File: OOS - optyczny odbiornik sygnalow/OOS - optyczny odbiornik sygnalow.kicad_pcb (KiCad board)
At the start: 2 copper layers, 25 x 50 mm, 45 parts, among them J101 Conn_Coaxial, J102 Conn_01x02_Socket, J103 Conn_01x02_Socket, J104 Conn_01x02_Socket, J105 Conn_01x02_Socket, U101 OPA300AIDBVR, U102 OPA300AIDBVR

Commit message: Polozenei komponentow na plycie, zdefiniowanie geometri, wczesny layout
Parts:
- removed C101, C104: 1p, Capacitor_SMD:C_0402_1005Metric
- removed C102: 2u2, Capacitor_SMD:C_0603_1608Metric
- removed C103: 100p, Capacitor_SMD:C_0402_1005Metric
- removed C105, C106: 1u, Resistor_SMD:R_0603_1608Metric
- removed C107, C108, C110: 100n, Resistor_SMD:R_0603_1608Metric
- removed C109, C111, C112: 10n, Capacitor_SMD:C_0402_1005Metric
- removed D101: BPX65, Package_TO_SOT_THT:TO-18-2_Lens
- removed D102, D103: LED, Diode_SMD:D_0603_1608Metric
- removed J101: Conn_Coaxial, Connector_Coaxial:BNC_Amphenol_B6252HB-NPP3G-50_Horizontal
- removed J102, J103, J104, J105: Conn_01x02_Socket, Connector_PinHeader_2.54mm:PinHeader_1x02_P2.54mm_Vertical
- removed JP101: SolderJumper_2_Open, Jumper:SolderJumper-2_P1.3mm_Bridged_RoundedPad1.0x1.5mm
- removed R101, R107, R108: 1k, Resistor_SMD:R_0402_1005Metric
- removed R102: 10, Resistor_SMD:R_0603_1608Metric
- removed R103, R104, R105, R109: 10k, Resistor_SMD:R_0402_1005Metric
- removed R106: 100, Resistor_SMD:R_0402_1005Metric
- removed R110: 10k, Resistor_SMD:R_0603_1608Metric
- removed R111: 2k2, Resistor_SMD:R_0603_1608Metric
- removed TP101, TP102, TP103, TP104, TP105, TP106, TP107, TP108, TP109, TP110, TP111: TestPoint_Small, TestPoint:TestPoint_Pad_D1.0mm
- removed U101, U102: OPA300AIDBVR, Package_TO_SOT_SMD:SOT-23-6_Handsoldering
- added C1: 1u, Resistor_SMD:R_0603_1608Metric, F.Cu at (194.3, 105.4)
- added C10: 1p, Capacitor_SMD:C_0402_1005Metric, F.Cu at (187.6, 102.4)
- added C11: 100p, Capacitor_SMD:C_0402_1005Metric, F.Cu at (187.1, 100.0)
- added C12: 1p, Capacitor_SMD:C_0402_1005Metric, F.Cu at (186.7, 89.4)
- added C2: 1u, Resistor_SMD:R_0603_1608Metric, F.Cu at (193.9, 93.9)
- added C3: 100n, Resistor_SMD:R_0603_1608Metric, F.Cu at (192.7, 105.4)
- added C4: 100n, Resistor_SMD:R_0603_1608Metric, F.Cu at (192.3, 93.9)
- added C5: 10n, Capacitor_SMD:C_0402_1005Metric, F.Cu at (191.4, 104.9)
- added C6: 10n, Capacitor_SMD:C_0402_1005Metric, F.Cu at (191.0, 93.4)
- added C7: 2u2, Capacitor_SMD:C_0603_1608Metric, F.Cu at (181.7, 108.3)
- added C8: 100n, Resistor_SMD:R_0603_1608Metric, F.Cu at (183.3, 108.3)
- added C9: 10n, Capacitor_SMD:C_0402_1005Metric, F.Cu at (184.6, 107.8)
- added D1: LED, Diode_SMD:D_0603_1608Metric, F.Cu at (179.8, 104.2)
- added D2: LED, Diode_SMD:D_0603_1608Metric, F.Cu at (197.2, 94.1)
- added D3: BPX65, Package_TO_SOT_THT:TO-18-2_Lens, F.Cu at (189.5, 110.1)
- added FID1: Fiducial, Fiducial:Fiducial_1.5mm_Mask3mm, F.Cu at (193.9, 115.4)
- added FID2: Fiducial, Fiducial:Fiducial_1.5mm_Mask3mm, F.Cu at (199.9, 82.9)
- added FID3: Fiducial, Fiducial:Fiducial_1.5mm_Mask3mm, F.Cu at (176.9, 82.9)
- added H1: MountingHole, MountingHole:MountingHole_3.2mm_M3, F.Cu at (176.9, 76.9)
- added H2: MountingHole, MountingHole:MountingHole_3.2mm_M3, F.Cu at (199.9, 76.9)
- added H3: MountingHole, MountingHole:MountingHole_3.2mm_M3, F.Cu at (199.9, 115.4)
- added H4: MountingHole, MountingHole:MountingHole_3.2mm_M3, F.Cu at (176.9, 115.4)
- added J1: Conn_01x02_Socket, Connector_PinHeader_2.54mm:PinHeader_1x02_P2.54mm_Vertical, F.Cu at (175.9, 107.0)
- added J2: Conn_01x02_Socket, Connector_PinHeader_2.54mm:PinHeader_1x02_P2.54mm_Vertical, F.Cu at (201.1, 97.0)
- added J3: Conn_01x02_Socket, Connector_PinHeader_2.54mm:PinHeader_1x02_P2.54mm_Vertical, F.Cu at (175.9, 97.0)
- added J4: Conn_01x02_Socket, Connector_PinHeader_2.54mm:PinHeader_1x02_P2.54mm_Vertical, F.Cu at (201.1, 107.0)
- added J5: Conn_Coaxial, Connector_Coaxial:BNC_Amphenol_B6252HB-NPP3G-50_Horizontal, F.Cu at (188.4, 84.5)
- added JP1: SolderJumper_2_Open, Jumper:SolderJumper-2_P1.3mm_Bridged_RoundedPad1.0x1.5mm, F.Cu at (201.1, 103.3)
- added R1: 10k, Resistor_SMD:R_0603_1608Metric, F.Cu at (176.7, 104.2)
- added R10: 1k, Resistor_SMD:R_0402_1005Metric, F.Cu at (187.2, 91.9)
- added R11: 1k, Resistor_SMD:R_0402_1005Metric, F.Cu at (188.1, 88.9)
- added R2: 2k2, Resistor_SMD:R_0603_1608Metric, F.Cu at (200.3, 94.1)
- added R3: 10, Resistor_SMD:R_0603_1608Metric, F.Cu at (179.4, 110.6)
- added R4: 10k, Resistor_SMD:R_0402_1005Metric, F.Cu at (198.8, 103.9)
- added R5: 10k, Resistor_SMD:R_0402_1005Metric, F.Cu at (182.9, 101.5)
- added R6: 10k, Resistor_SMD:R_0402_1005Metric, F.Cu at (182.9, 100.4)
- added R7: 10k, Resistor_SMD:R_0402_1005Metric, F.Cu at (182.9, 99.3)
- added R8: 1k, Resistor_SMD:R_0402_1005Metric, F.Cu at (187.6, 103.4)
- added R9: 100, Resistor_SMD:R_0402_1005Metric, F.Cu at (187.6, 97.4)
- added TP1: TestPoint_Small, TestPoint:TestPoint_Pad_D1.0mm, F.Cu at (178.6, 109.2)
- added TP10: TestPoint_Small, TestPoint:TestPoint_Pad_D1.0mm, F.Cu at (186.7, 90.9)
- added TP11: TestPoint_Small, TestPoint:TestPoint_Pad_D1.0mm, F.Cu at (186.7, 87.9)
- added TP2: TestPoint_Small, TestPoint:TestPoint_Pad_D1.0mm, F.Cu at (185.2, 110.1)
- added TP3: TestPoint_Small, TestPoint:TestPoint_Pad_D1.0mm, F.Cu at (184.2, 102.4)
- added TP4: TestPoint_Small, TestPoint:TestPoint_Pad_D1.0mm, F.Cu at (184.9, 98.6)
- added TP5: TestPoint_Small, TestPoint:TestPoint_Pad_D1.0mm, F.Cu at (196.8, 103.9)
- added TP6: TestPoint_Small, TestPoint:TestPoint_Pad_D1.0mm, F.Cu at (189.5, 108.4)
- added TP7: TestPoint_Small, TestPoint:TestPoint_Pad_D1.0mm, F.Cu at (187.1, 101.4)
- added TP8: TestPoint_Small, TestPoint:TestPoint_Pad_D1.0mm, F.Cu at (187.1, 98.5)
- added TP9: TestPoint_Small, TestPoint:TestPoint_Pad_D1.0mm, F.Cu at (189.4, 96.6)
- added U1: OPA300AIDBVR, Package_TO_SOT_SMD:SOT-23-6_Handsoldering, F.Cu at (188.4, 105.8)
- added U2: OPA300AIDBVR, Package_TO_SOT_SMD:SOT-23-6_Handsoldering, F.Cu at (188.0, 94.3)
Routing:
- net +5V: track 0.00 -> 26.2 mm
- net /OPA300_En: track 0.00 -> 26.0 mm
- net +V_photo: track 0.00 -> 9.94 mm
- net /BPX65_Cathode: track 0.00 -> 9.66 mm
- net /OPA300_TIA_+: track 0.00 -> 8.66 mm
- net /OPA300_x10_+: track 0.00 -> 8.57 mm
- net /OPA300_TIA_-: track 0.00 -> 7.98 mm
- net /OPA300_x10_-: track 0.00 -> 7.65 mm
- net /OPA300_En_Alt_Con: track 0.00 -> 7.43 mm
- net /OPA300_x10_Out_AC: track 0.00 -> 6.11 mm
- net /OPA300_TIA_Out: track 0.00 -> 4.37 mm
- net /OPA300_x10_Out: track 0.00 -> 3.47 mm
- net /OPA300_TIA_Out_AC: track 0.00 -> 2.12 mm
- net Net-(D1-A): track 0.00 -> 1.49 mm
- net Net-(D2-A): track 0.00 -> 1.45 mm
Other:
- board size 25 x 50 mm -> 31 x 47 mm

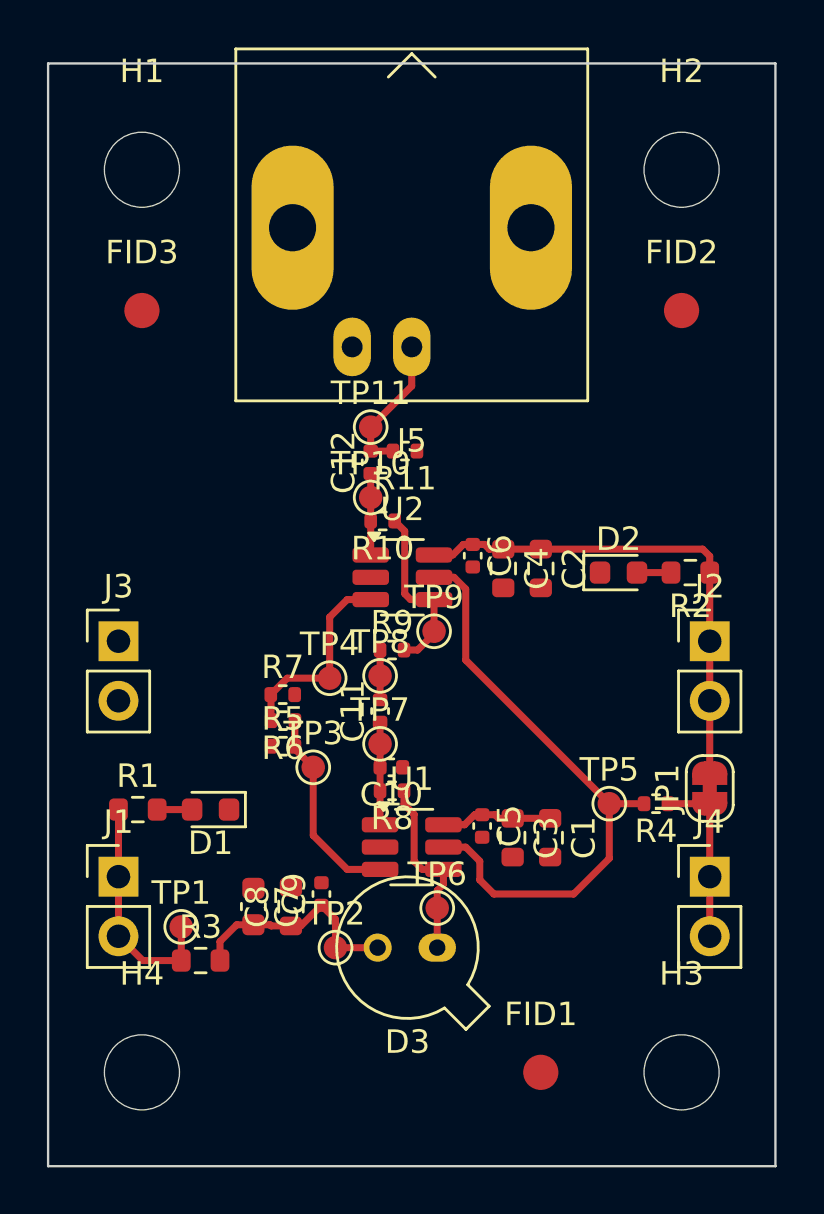
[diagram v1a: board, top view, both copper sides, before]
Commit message: Wstepne polaczenie komponentow, ustawienie plaszczyzny masy, ustalenie 2 warstw plytki
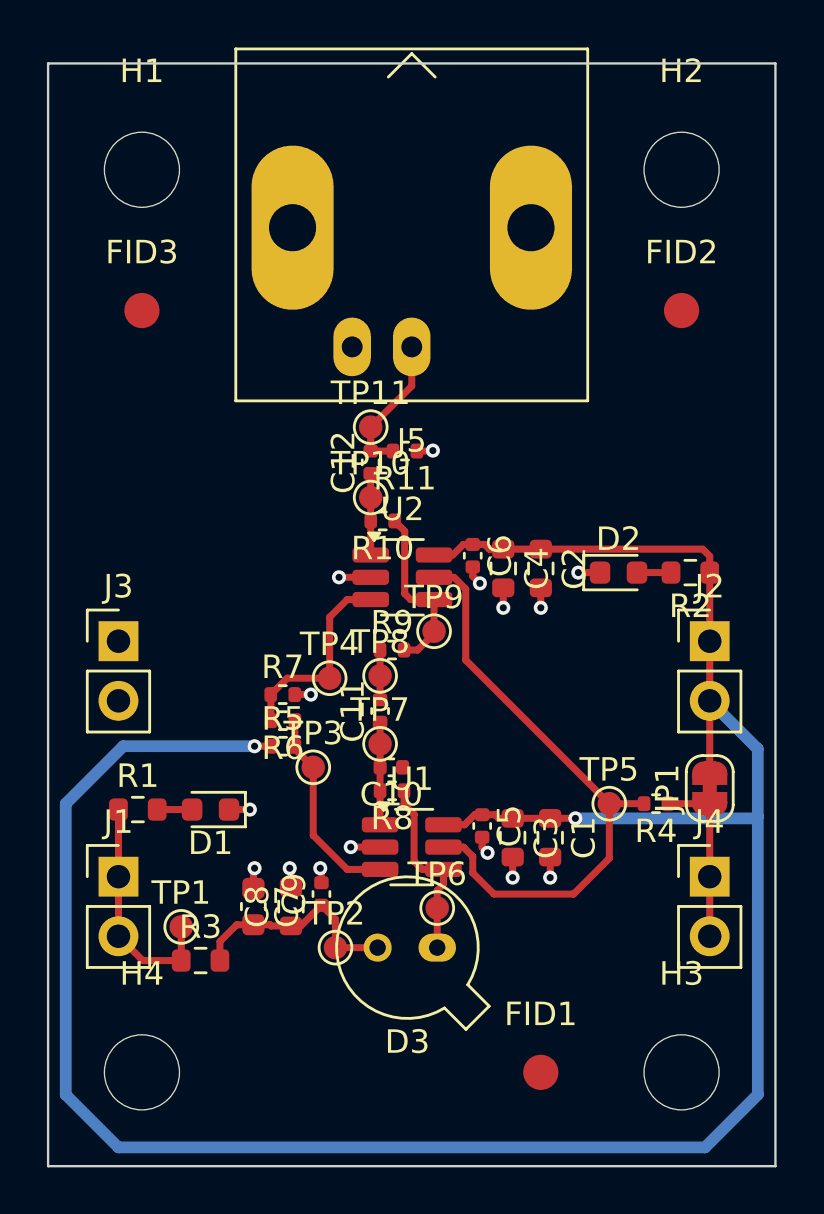
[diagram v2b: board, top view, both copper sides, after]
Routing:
- net +5V: track 26.2 -> 106.2 mm, vias 0 -> 2
- net 0V: track 0.00 -> 13.2 mm, vias 0 -> 15
- added copper zone on B.Cu, net 0V

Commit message: Polozenie komponentow, layout w wersji 0.0
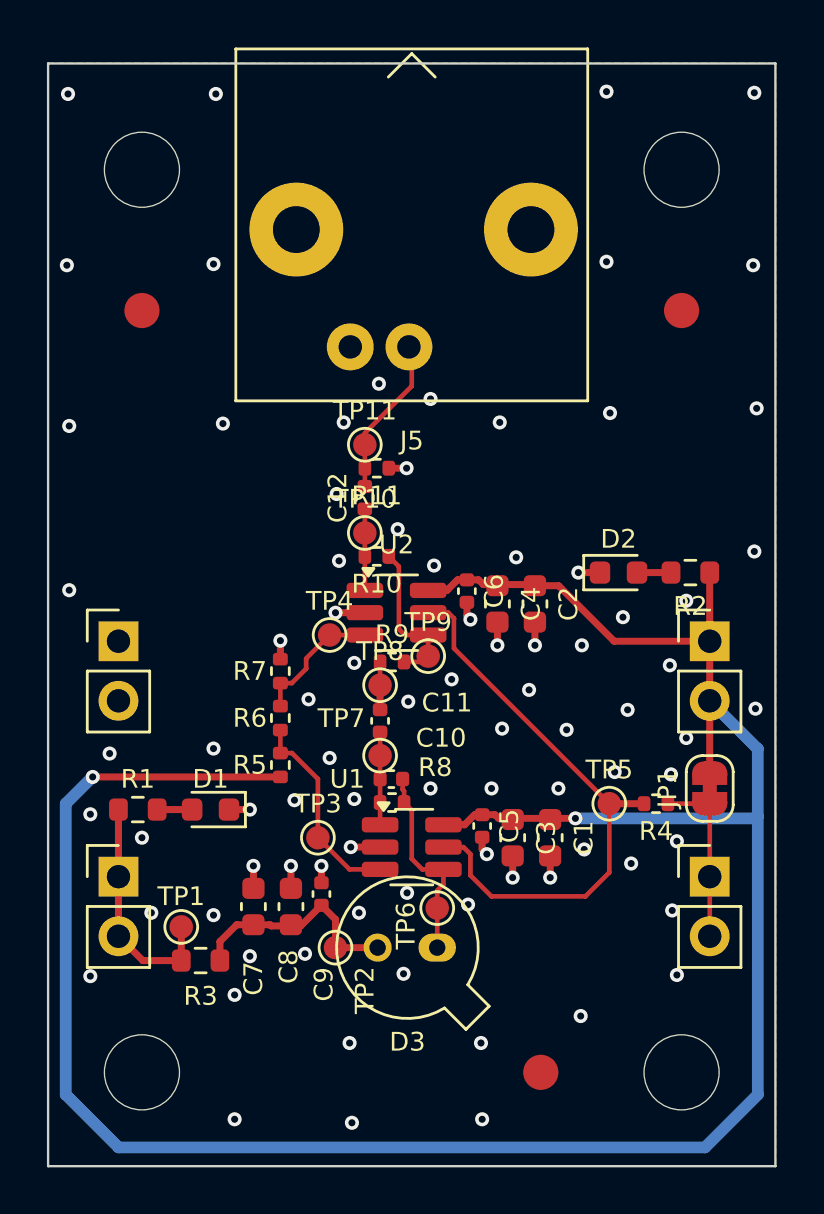
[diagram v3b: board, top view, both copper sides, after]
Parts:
- C1, C2, C3, C4, C8: footprint Resistor_SMD:R_0603_1608Metric -> Capacitor_SMD:C_0603_1608Metric
- moved TP3 3.01 mm to (184.4, 105.4)
- moved TP4 1.84 mm to (184.9, 96.7)
- moved C12 1.53 mm to (186.4, 90.9)
- moved C2 1.53 mm to (193.7, 95.4)
- moved C4 1.53 mm to (192.1, 95.4)
- moved C6 1.53 mm to (190.8, 94.9)
- moved R10 1.53 mm to (186.9, 93.4)
- moved TP10 1.53 mm to (186.4, 92.4)
- moved U2 1.53 mm to (187.8, 95.8)
- moved R11 1.40 mm to (186.9, 89.6)
- moved TP9 1.09 mm to (189.1, 97.6)
- moved R7 1.00 mm to (182.8, 98.3), turned to 90 degrees
- moved R5 0.81 mm to (182.8, 102.3), turned to 90 degrees
- moved TP11 0.79 mm to (186.4, 88.6)
- moved R9 0.51 mm to (187.6, 97.9)
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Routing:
- net /OPA300_x10_+: track 8.57 -> 5.69 mm
- net /OPA300_x10_-: track 7.65 -> 6.58 mm
- net /OPA300_En: track 26.0 -> 25.1 mm
- net /OPA300_x10_Out_AC: track 6.11 -> 6.78 mm
- net /OPA300_TIA_-: track 7.98 -> 8.54 mm
- net 0V: track 13.2 -> 13.7 mm, vias 15 -> 85
- added copper zone on F.Cu, net 0V
